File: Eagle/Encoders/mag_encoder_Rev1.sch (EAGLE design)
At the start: 7 parts, among them IC1 A1203LH

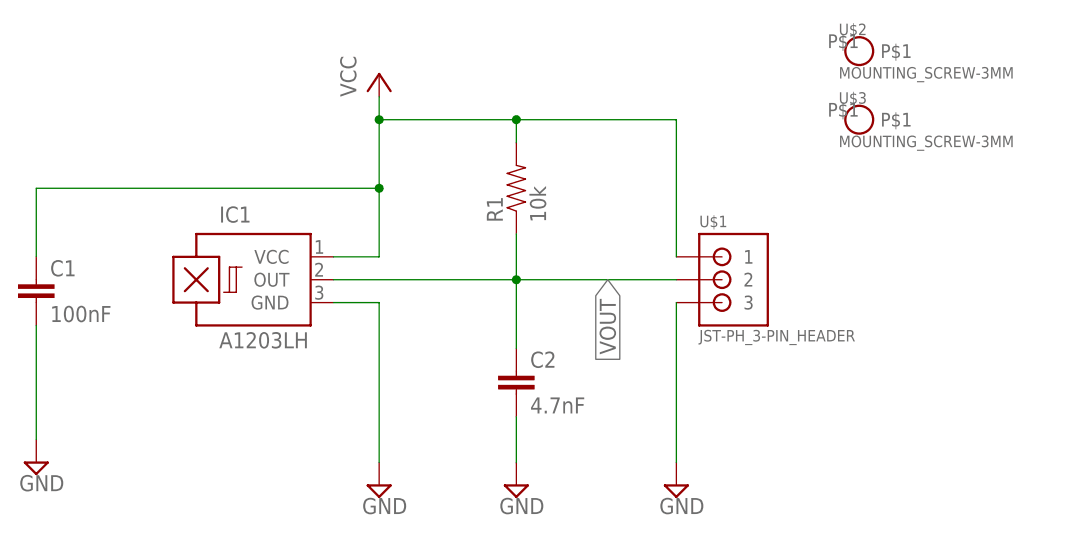
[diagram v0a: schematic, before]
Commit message: Modified encoder board designs.
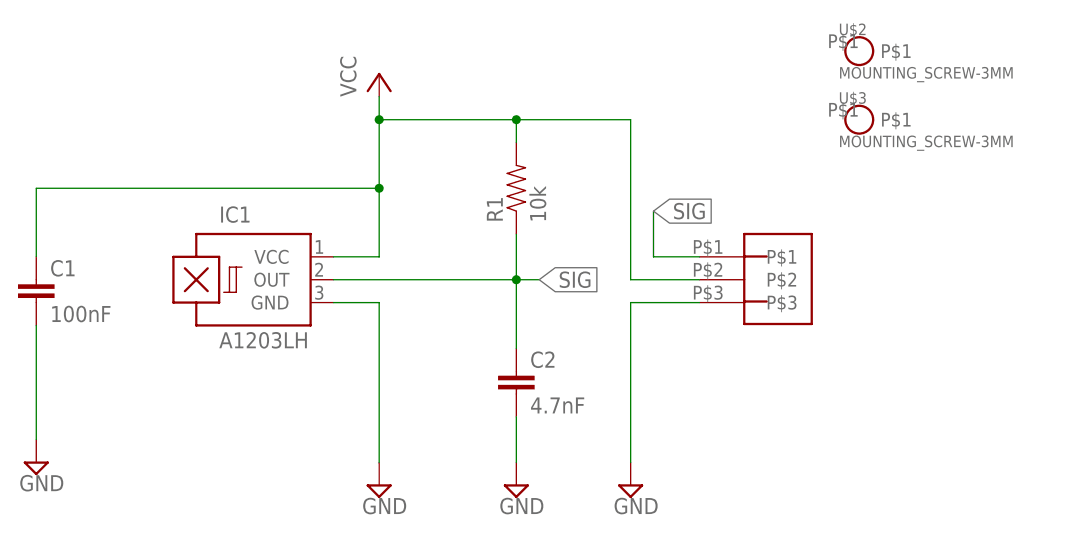
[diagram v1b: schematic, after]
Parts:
- U$1: value JST-PH_3-PIN_HEADER -> 3_PIN_JST-XH; device Clayton:JST-PH_3-PIN_HEADER -> Clayton:3_PIN_JST-XH
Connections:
- removed net VOUT: C2.1, IC1.OUT, R1.1, U$1.2
- removed net WIRE: C1.1, IC1.VCC, R1.2, U$1.1
- new net SIG: C2.1, IC1.OUT, R1.1, U$1.P$1
- new net VCC: C1.1, IC1.VCC, R1.2, U$1.P$2
- net GND: now also U$1.P$3; no longer U$1.3
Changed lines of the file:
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@@
 <part name="SUPPLY2" library="supply2" deviceset="GND" device=""/>
 <part name="SUPPLY3" library="supply2" deviceset="GND" device=""/>
-<part name="U$1" library="Clayton" deviceset="JST-PH_3-PIN_HEADER" device=""/>
-<part name="SUPPLY4" library="supply2" deviceset="GND" device=""/>
 <part name="U$2" library="Clayton" deviceset="MOUNTING_SCREW-3MM" device=""/>
 <part name="U$3" library="Clayton" deviceset="MOUNTING_SCREW-3MM" device=""/>
+<part name="U$1" library="Clayton" deviceset="3_PIN_JST-XH" device=""/>
+<part name="SUPPLY4" library="supply2" deviceset="GND" device=""/>
 </parts>
 <sheets>
@@
 <instance part="SUPPLY2" gate="GND" x="17.78" y="40.64"/>
 <instance part="SUPPLY3" gate="GND" x="71.12" y="38.1"/>
-<instance part="U$1" gate="G$1" x="93.98" y="60.96"/>
-<instance part="SUPPLY4" gate="GND" x="88.9" y="38.1"/>
 <instance part="U$2" gate="G$1" x="109.22" y="86.36"/>
 <instance part="U$3" gate="G$1" x="109.22" y="78.74"/>
+<instance part="U$1" gate="G$1" x="91.44" y="66.04" rot="R270"/>
+<instance part="SUPPLY4" gate="GND" x="83.82" y="38.1"/>
 </instances>
 <busses>
 </busses>
 <nets>
-<net name="VOUT" class="0">
-<segment>
-<pinref part="IC1" gate="G$1" pin="OUT"/>
-<wire x1="50.8" y1="60.96" x2="71.12" y2="60.96" width="0.1524" layer="91"/>
-<pinref part="C2" gate="G$1" pin="1"/>
-<wire x1="71.12" y1="60.96" x2="88.9" y2="60.96" width="0.1524" layer="91"/>
-<wire x1="71.12" y1="53.34" x2="71.12" y2="60.96" width="0.1524" layer="91"/>
-<junction x="71.12" y="60.96"/>
-<pinref part="R1" gate="G$1" pin="1"/>
-<wire x1="71.12" y1="66.04" x2="71.12" y2="60.96" width="0.1524" layer="91"/>
-<label x="81.28" y="60.96" size="1.778" layer="95" rot="R270" xref="yes"/>
-<pinref part="U$1" gate="G$1" pin="2"/>
-</segment>
-</net>
 <net name="GND" class="0">
 <segment>
@@
 </segment>
 <segment>
-<pinref part="U$1" gate="G$1" pin="3"/>
+<pinref part="U$1" gate="G$1" pin="P$3"/>
+<wire x1="91.44" y1="58.42" x2="83.82" y2="58.42" width="0.1524" layer="91"/>
 <pinref part="SUPPLY4" gate="GND" pin="GND"/>
-<wire x1="88.9" y1="58.42" x2="88.9" y2="40.64" width="0.1524" layer="91"/>
+<wire x1="83.82" y1="58.42" x2="83.82" y2="40.64" width="0.1524" layer="91"/>
 </segment>
 </net>
-<net name="WIRE" class="0">
+<net name="VCC" class="0">
 <segment>
-<pinref part="U$1" gate="G$1" pin="1"/>
-<wire x1="88.9" y1="63.5" x2="88.9" y2="78.74" width="0.1524" layer="91"/>
 <pinref part="C1" gate="G$1" pin="1"/>
 <wire x1="17.78" y1="63.5" x2="17.78" y2="71.12" width="0.1524" layer="91"/>
@@
 <wire x1="17.78" y1="71.12" x2="55.88" y2="71.12" width="0.1524" layer="91"/>
 <junction x="55.88" y="71.12"/>
-<wire x1="88.9" y1="78.74" x2="71.12" y2="78.74" width="0.1524" layer="91"/>
 <junction x="71.12" y="78.74"/>
+<pinref part="U$1" gate="G$1" pin="P$2"/>
+<wire x1="83.82" y1="78.74" x2="71.12" y2="78.74" width="0.1524" layer="91"/>
+<wire x1="91.44" y1="60.96" x2="83.82" y2="60.96" width="0.1524" layer="91"/>
+<wire x1="83.82" y1="60.96" x2="83.82" y2="78.74" width="0.1524" layer="91"/>
+</segment>
+</net>
+<net name="SIG" class="0">
+<segment>
+<pinref part="IC1" gate="G$1" pin="OUT"/>
+<wire x1="50.8" y1="60.96" x2="71.12" y2="60.96" width="0.1524" layer="91"/>
+<pinref part="C2" gate="G$1" pin="1"/>
+<wire x1="71.12" y1="53.34" x2="71.12" y2="60.96" width="0.1524" layer="91"/>
+<junction x="71.12" y="60.96"/>
+<pinref part="R1" gate="G$1" pin="1"/>
+<wire x1="71.12" y1="66.04" x2="71.12" y2="60.96" width="0.1524" layer="91"/>
+<wire x1="71.12" y1="60.96" x2="73.66" y2="60.96" width="0.1524" layer="91"/>
+<label x="73.66" y="60.96" size="1.778" layer="95" xref="yes"/>
+</segment>
+<segment>
+<pinref part="U$1" gate="G$1" pin="P$1"/>
+<wire x1="91.44" y1="63.5" x2="86.36" y2="63.5" width="0.1524" layer="91"/>
+<wire x1="86.36" y1="63.5" x2="86.36" y2="68.58" width="0.1524" layer="91"/>
+<label x="86.36" y="68.58" size="1.778" layer="95" xref="yes"/>
 </segment>
 </net>
@@
 </sheet>
 </sheets>
+<errors>
+</errors>
 </schematic>
 </drawing>
